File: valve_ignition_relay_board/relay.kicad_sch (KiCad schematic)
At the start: 33 parts, among them J2 ACT_PWR, J3 ACT_PWR, J4 Actuator, Q1 MMBF170, Q2 MMBF170, U3 G5LE-1A4, U4 RT424012F, U7 INA180, U8 INA180

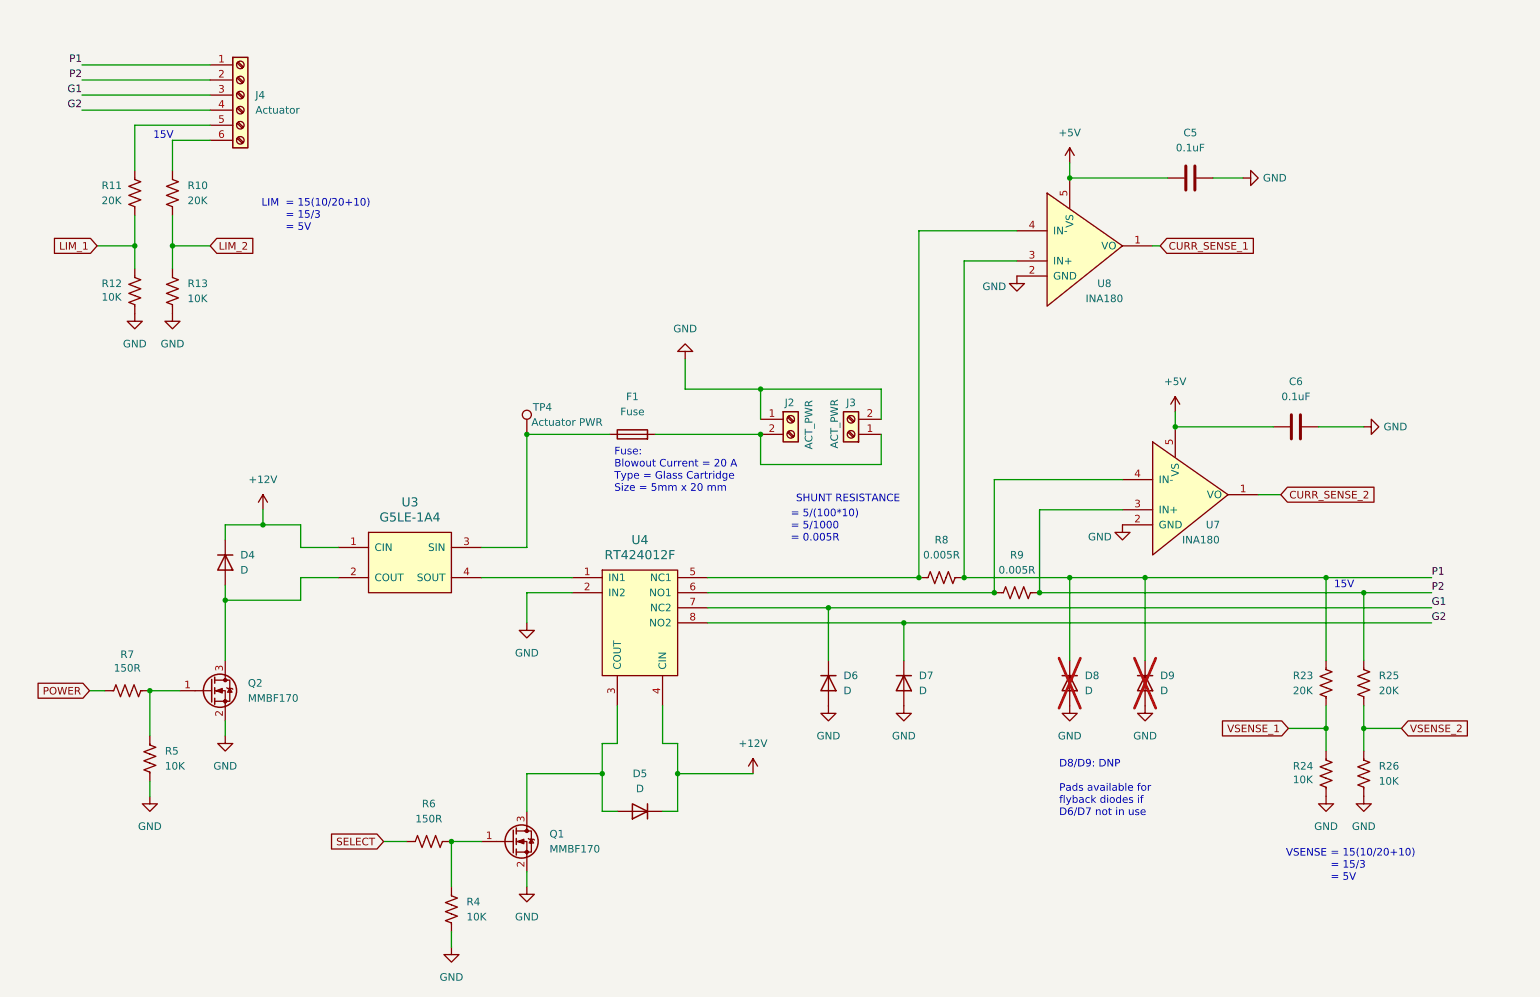
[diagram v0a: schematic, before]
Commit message: Valve Ignition Relay - ready for review 1
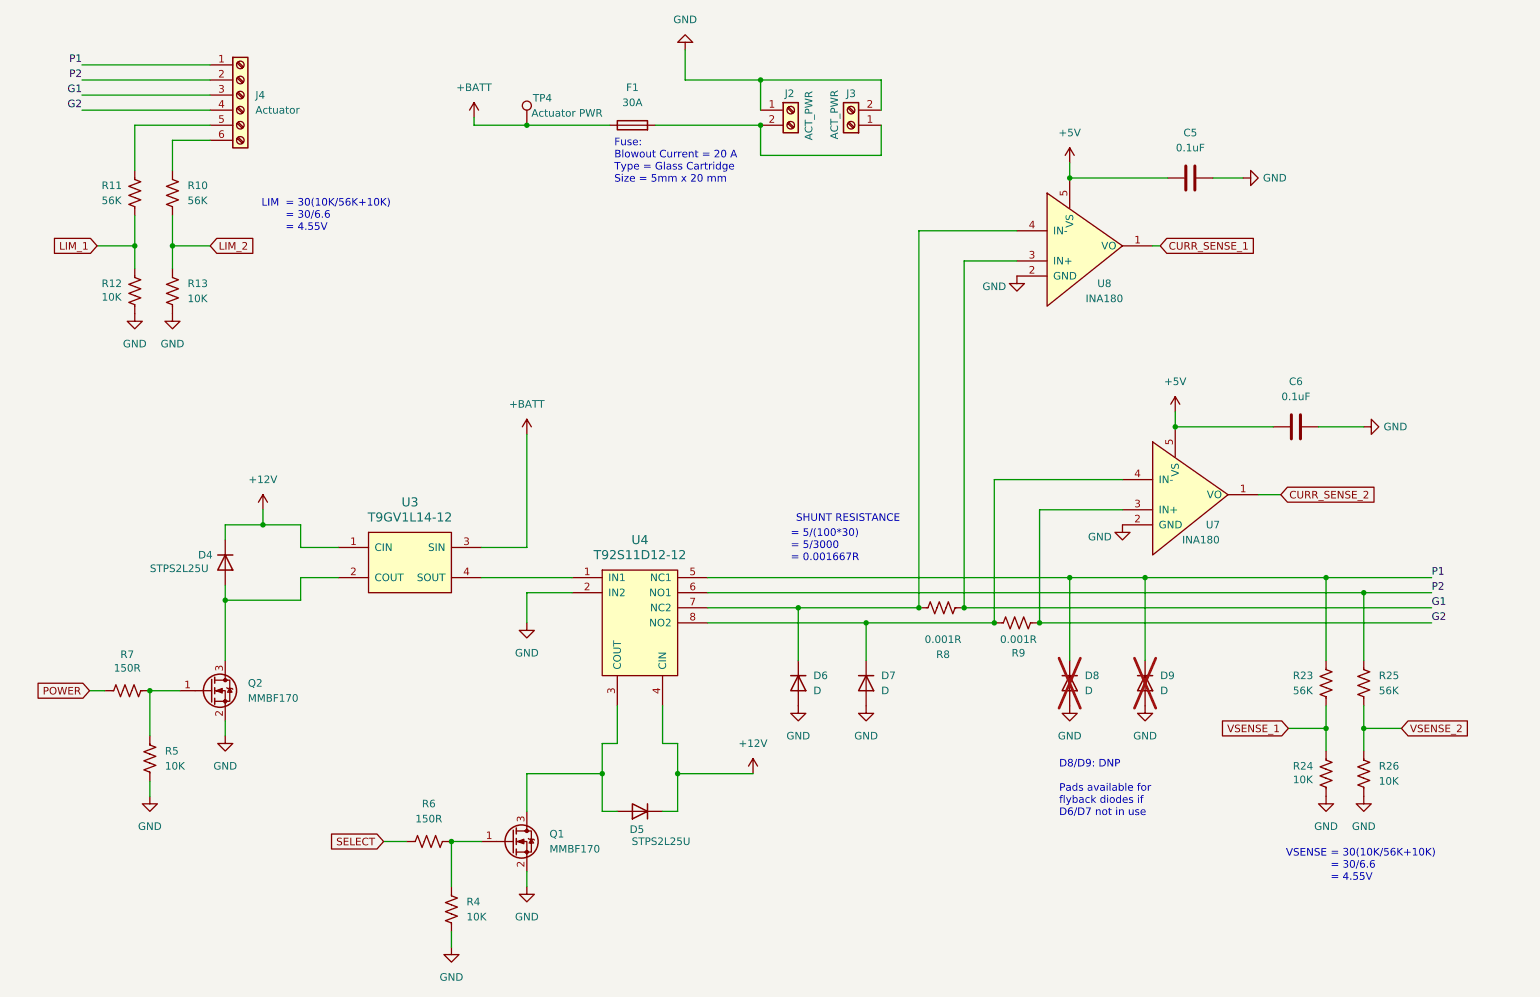
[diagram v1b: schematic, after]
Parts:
- D4, D5: value D -> STPS2L25U
- F1: value Fuse -> 30A; footprint (none) -> footprints:3557-10_KEY
- R10, R11, R23, R25: value 20K -> 56K
- R8, R9: value 0.005R -> 0.001R
- TP4: footprint (none) -> TestPoint:TestPoint_Keystone_5000-5004_Miniature
- U3: value G5LE-1A4 -> T9GV1L14-12; footprint (none) -> footprints:T9GV1L1412
- U4: value RT424012F -> T92S11D12-12; footprint (none) -> footprints:RELAY8-T92-MODULE
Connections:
- net G1: now also R8.2, U8.3 (IN+); no longer D6.1 (K), U4.7 (NC2)
- net G2: now also R9.2, U7.3 (IN+); no longer D7.1 (K), U4.8 (NO2)
- net P1: now also U4.5 (NC1); no longer R8.2, U8.3 (IN+)
- net P2: now also U4.6 (NO1); no longer R9.2, U7.3 (IN+)
- net +BATT: now reaches F1.1, TP4.1, U3.3 (SIN)
- net at R8.1, U8.4 (IN-): now also D6.1 (K), U4.7 (NC2); no longer U4.5 (NC1)
- net at R9.1, U7.4 (IN-): now also D7.1 (K), U4.8 (NO2); no longer U4.6 (NO1)
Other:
- note added: "= 30(10K/56K+10K) = 30/6.6 = 4.55V"
- note added: "= 5/(100*30) = 5/3000 = 0.001667R"
- note removed: "15V"
- note removed: "= 15(10/20+10) = 15/3 = 5V"
- note removed: "= 5/(100*10) = 5/1000 = 0.005R"
- moved on the sheet: D6, D7, F1, J2, J3, R8, R9, TP4

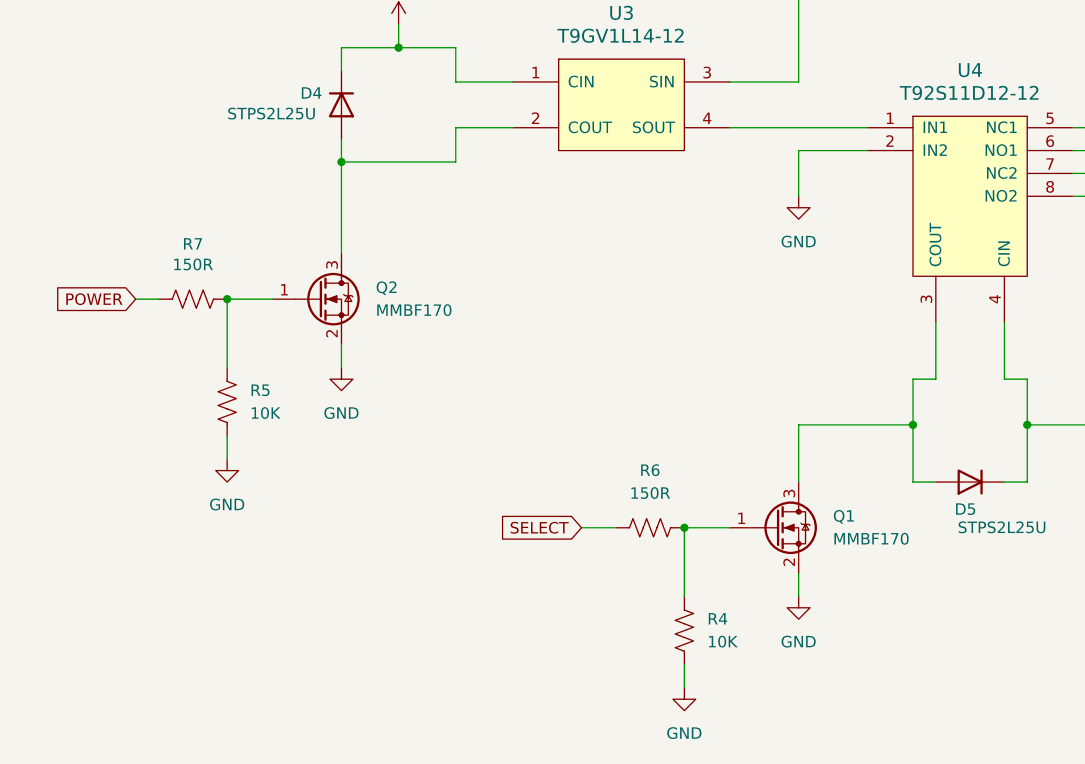
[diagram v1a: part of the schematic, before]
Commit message: Replaced MOSFETs with optoisolators
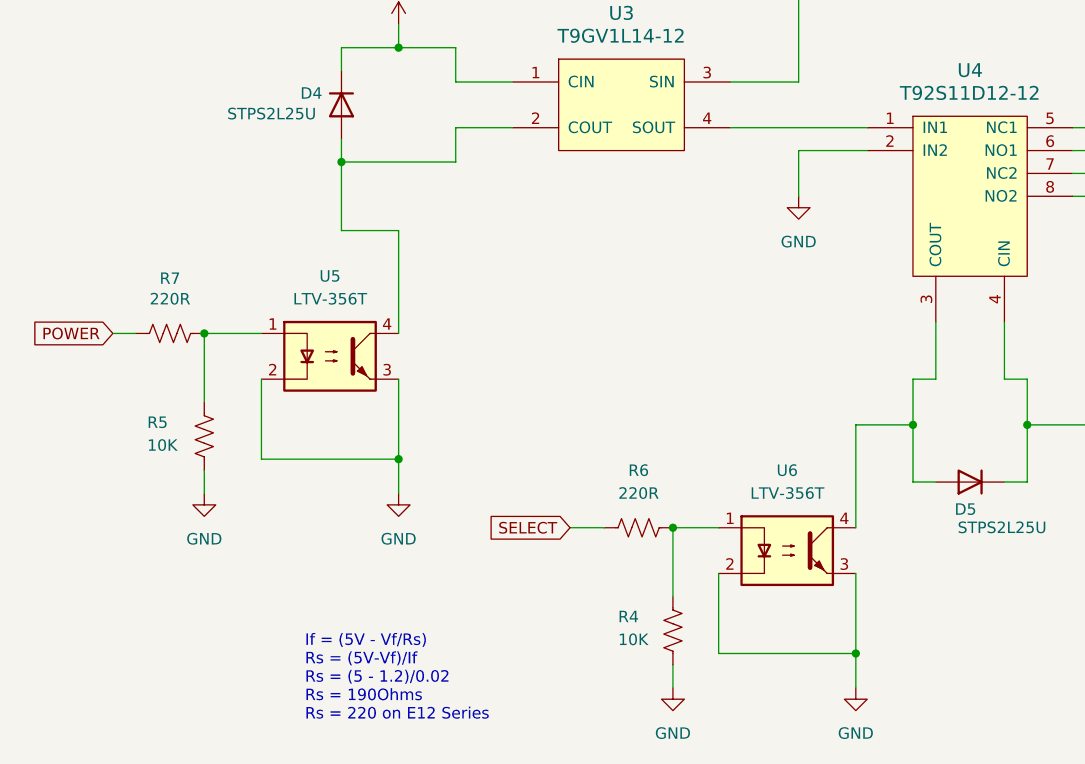
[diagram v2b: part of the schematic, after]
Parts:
- removed Q1, Q2: MMBF170, Package_TO_SOT_SMD:SOT-23, symbol Transistor_FET:MMBF170
- added U5, U6: LTV-356T, Package_SO:SO-4_4.4x3.6mm_P2.54mm, symbol Isolator:LTV-356T
- R6, R7: value 150R -> 220R
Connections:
- net GND: now also U5.2, U5.3, U6.2, U6.3
- net at R4.1, R6.2: now also U6.1
- net at D5.2 (A), U4.3 (COUT): now also U6.4
- net at R5.1, R7.2: now also U5.1
- net at D4.2 (A), U3.2 (COUT): now also U5.4
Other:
- note added: "If = (5V - Vf/Rs) Rs = (5V-Vf)/If Rs = (5 - 1.2)/0.02 Rs = 190Ohms Rs = 220 on E12 Series"
- moved on the sheet: R4, R5, R6, R7

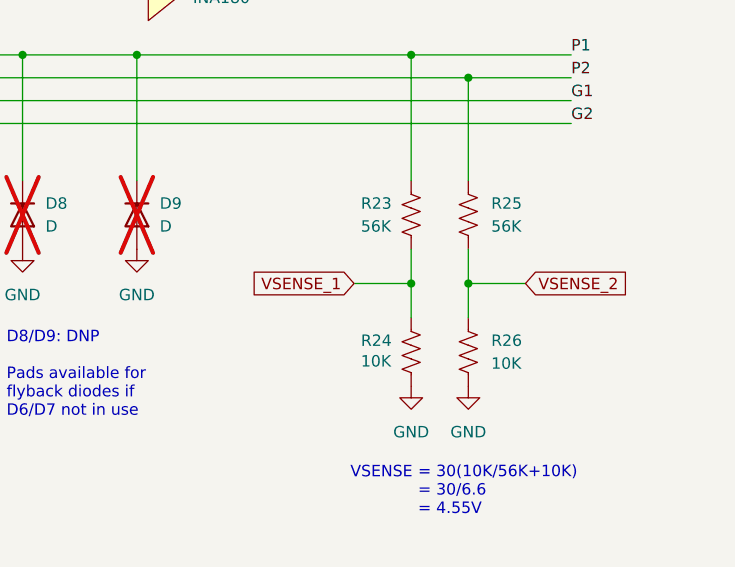
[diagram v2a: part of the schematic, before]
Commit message: Added IO Expander and moved dip switch
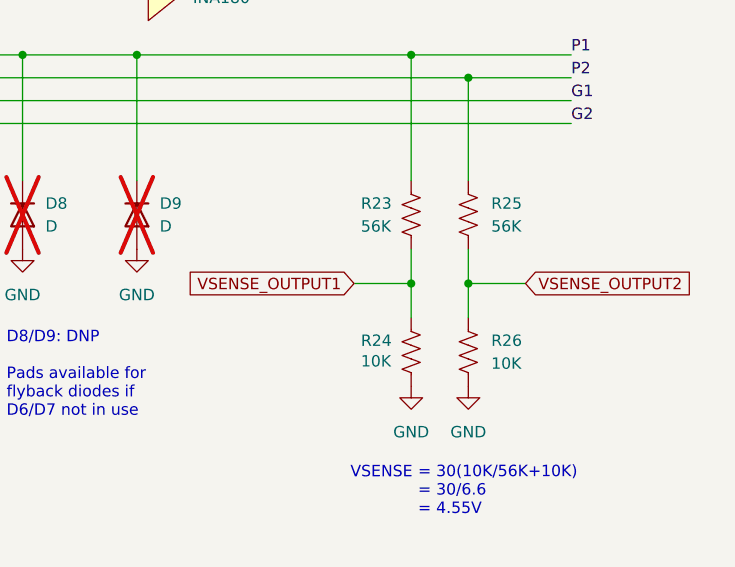
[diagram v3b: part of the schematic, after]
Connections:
- net VSENSE_1 renamed VSENSE_OUTPUT1
- net VSENSE_2 renamed VSENSE_OUTPUT2
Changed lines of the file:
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@@
 		)
 	)
-	(global_label "VSENSE_2"
+	(global_label "VSENSE_OUTPUT2"
 		(shape input)
 		(at 248.92 138.43 0)
@@
 		)
 		(property "Intersheetrefs" "${INTERSHEET_REFS}"
-			(at 261.2184 138.43 0)
+			(at 268.4151 138.43 0)
 			(effects
 				(font
@@
 		)
 	)
-	(global_label "VSENSE_1"
+	(global_label "VSENSE_OUTPUT1"
 		(shape input)
 		(at 229.87 138.43 180)
@@
 		)
 		(property "Intersheetrefs" "${INTERSHEET_REFS}"
-			(at 217.5716 138.43 0)
+			(at 210.3749 138.43 0)
 			(effects
 				(font

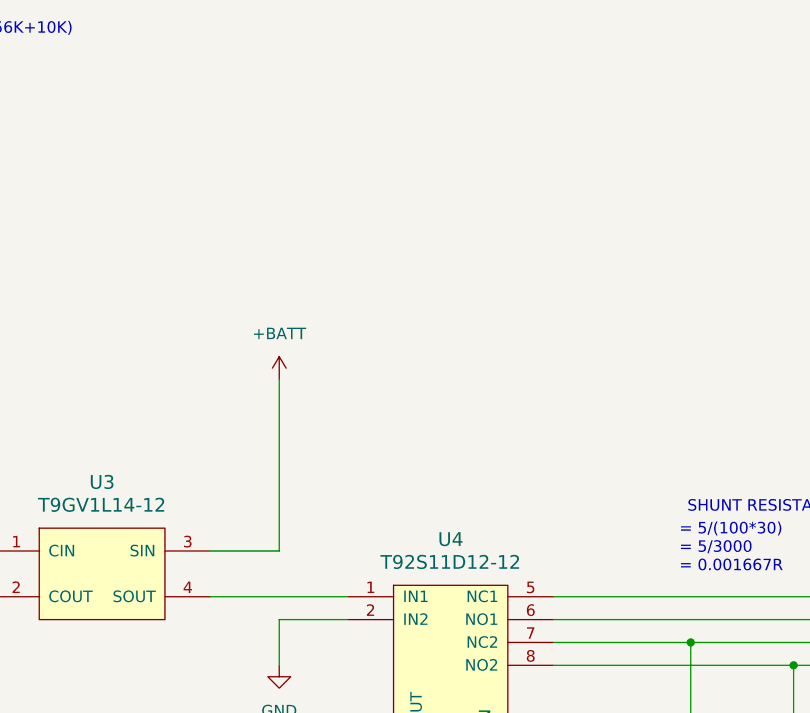
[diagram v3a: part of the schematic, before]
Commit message: Added 4 new signals to the microcontroller
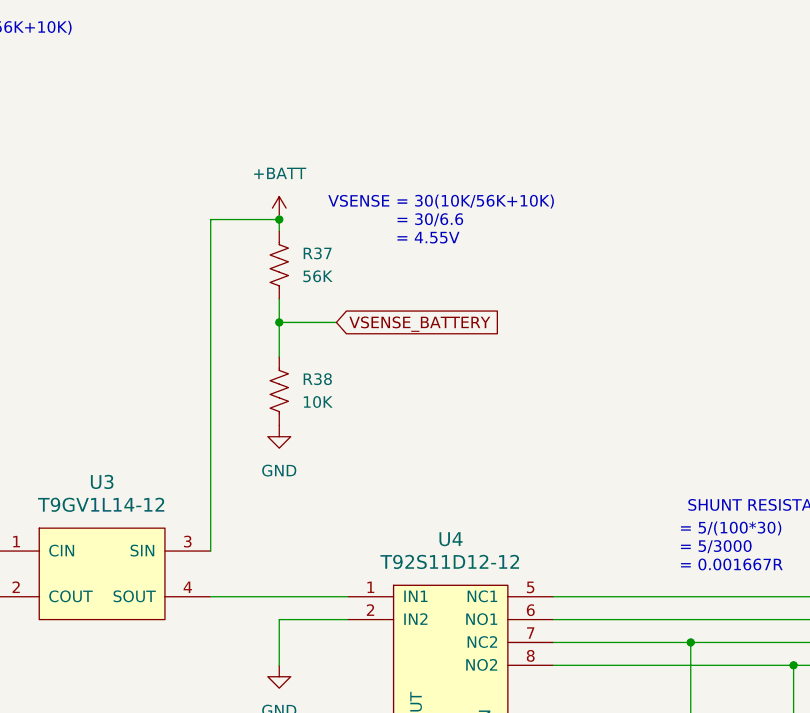
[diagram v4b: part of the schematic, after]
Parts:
- added R37: 56K, Resistor_SMD:R_0805_2012Metric_Pad1.20x1.40mm_HandSolder, symbol Device:R_US
- added R38: 10K, Resistor_SMD:R_0805_2012Metric_Pad1.20x1.40mm_HandSolder, symbol Device:R_US
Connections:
- net +BATT: now also R37.2
- net GND: now also R38.1
- new net VSENSE_BATTERY: R37.1, R38.2
